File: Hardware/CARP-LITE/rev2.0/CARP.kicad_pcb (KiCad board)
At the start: 4 copper layers, 70.1 x 40 mm, 155 parts, among them J1 USB-C, J10 PYRO_2, J11 RF_L, J12 PYRO_2_B, J13 PYRO_1_B, J3 I2C1+3V3, J4 2/3S XT30, J5 UART+5V+I2C1, J6 PYRO_1, J7 SPI, J8 PWM1+5V1, J9 PWM2+5V1, Q5 SQ2318CES, Q6 SQ2318CES, Q7 SQ2318CES, SW1 SW_Push, SW2 SW_Push, U1 BQ25792, U10 TPS62130A, U2 W25Q128JVSIMTR (16MB), U3 BMP581, U4 RP2350_60QFN, U5 LSM6DSO, U7 TLV75733PDBV, U9 LR2021IMLTRT, Y1 ABM8-272-T3, Y2 ECS-TXO-25CSMV-320-AN-TR

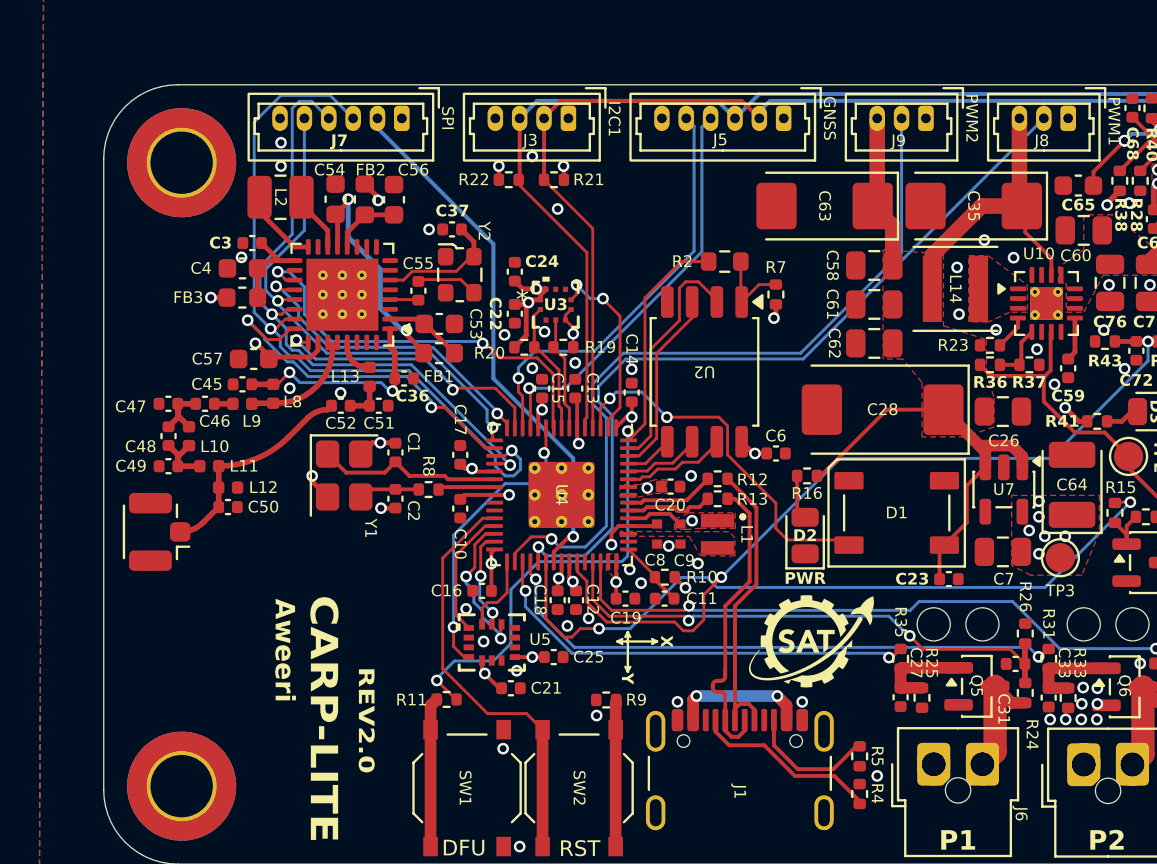
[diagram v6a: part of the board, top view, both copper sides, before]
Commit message: extra connector
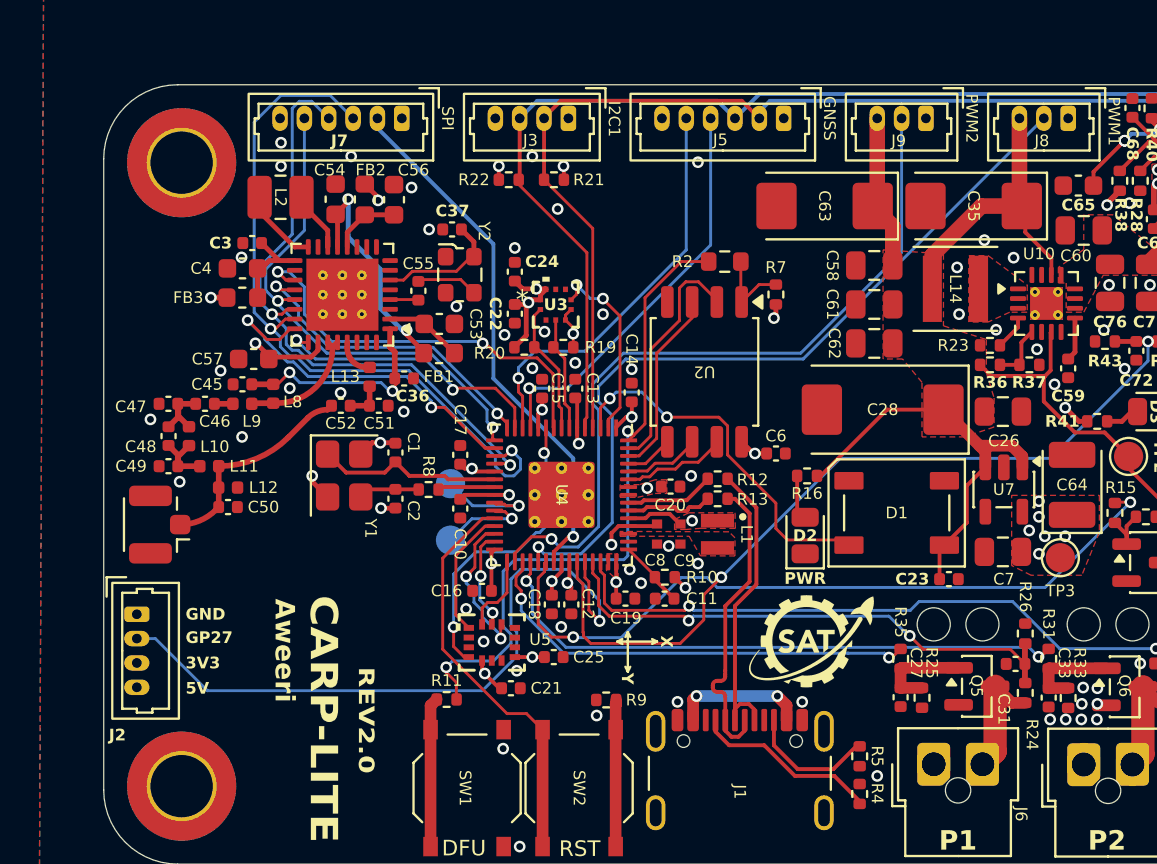
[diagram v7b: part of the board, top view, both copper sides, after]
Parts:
- added J2: Extra Connection, Connector_Molex:Molex_PicoBlade_53047-0410_1x04_P1.25mm_Vertical, F.Cu at (102.3, 102.4)
- added TP1: SWCLK, TestPoint:TestPoint_Pad_D1.5mm, B.Cu at (118.4, 95.7)
- added TP4: SWD, TestPoint:TestPoint_Pad_D1.5mm, B.Cu at (118.4, 98.6)
- moved J11 0.38 mm to (103.0, 97.8)
- moved C18 0.37 mm to (123.6, 101.9)
- moved C12 0.33 mm to (124.6, 101.9)
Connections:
- U4 pad 41: unconnected-(U4-GPIO27_ADC1-Pad41) -> /GPIO27_ADC1
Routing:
- net +5V: track 104.8 -> 143.8 mm
- net /GPIO27_ADC1: track 0.00 -> 35.2 mm, vias 0 -> 1
- net /SWCLK: track 0.00 -> 5.29 mm, vias 0 -> 1
- net /SWD: track 0.00 -> 4.67 mm, vias 0 -> 1
- net /GPIO26_ADC0: track 41.4 -> 43.0 mm
- net /QSPI_SS: track 34.0 -> 34.8 mm
- net /GPIO24: track 37.4 -> 38.1 mm
- net /GPIO9: track 21.7 -> 21.1 mm
- net /RUN: track 21.6 -> 21.0 mm
- net /GPIO20: track 39.3 -> 38.7 mm
- net /GPIO21: track 22.9 -> 23.4 mm
- net GND: vias 61 -> 71
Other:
- board text added: "3V3"
- board text added: "5V"
- board text added: "GND"
- board text added: "GP27"
- board text added: "SWCLK"
- board text added: "SWD"
